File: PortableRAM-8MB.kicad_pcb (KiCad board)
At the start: 4 copper layers, 123 x 81 mm, 34 parts, among them J1 RAM Connector, J2 JTAG_Header_2.54mm_1x06, U1 ATF1502ASL, U10 AMS1117-3.3, U11 74HC245, U12 74HC245, U2 IS61WV5128BLL-10TLI, U3 IS61WV5128BLL-10TLI, U4 IS61WV5128BLL-10TLI, U5 IS61WV5128BLL-10TLI, U6 IS61WV5128BLL-10TLI, U7 IS61WV5128BLL-10TLI, U8 IS61WV5128BLL-10TLI, U9 IS61WV5128BLL-10TLI

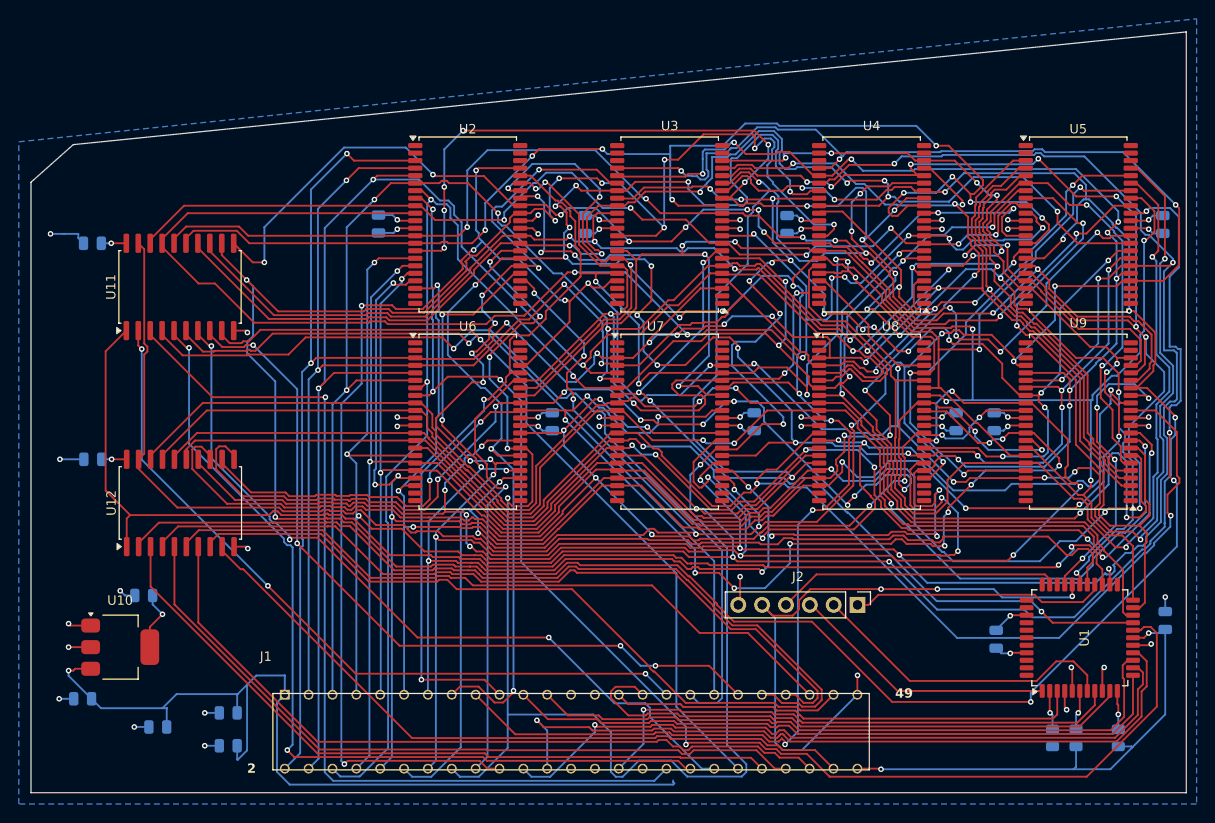
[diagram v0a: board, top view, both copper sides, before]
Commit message: PCB: strip all routing for fresh v2 layout, fix planes for all-5V
Clean canvas: all tracks and vias deleted; B.Cu +5V pour removed
(bottom layer freed for routing); In2 plane retargeted +3.3V -> +5V.
Preserved: proven board outline + angled corner, J1 position, the
edge-connector keepout, In1 GND plane, and all footprint placements
as a starting point. Next: Update PCB from Schematic, re-place as
needed, edge keepout, route.

Co-Authored-By: Claude Fable 5 <noreply@anthropic.com>
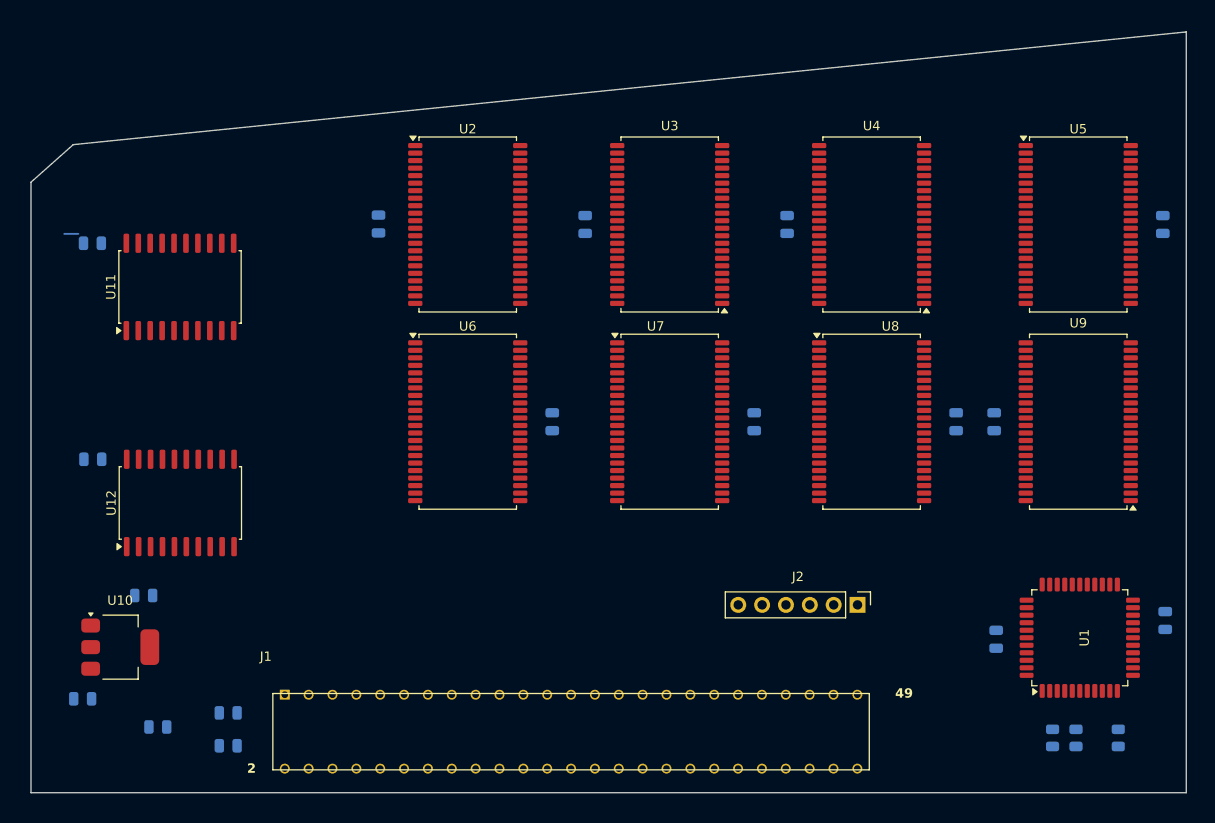
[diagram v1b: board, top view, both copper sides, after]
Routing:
- net /A13: track 316.4 -> 0.00 mm, vias 19 -> 0
- net /SD6: track 290.5 -> 0.00 mm, vias 13 -> 0
- net /A15: track 289.0 -> 0.00 mm, vias 23 -> 0
- net /A6: track 287.1 -> 0.00 mm, vias 12 -> 0
- net /A11: track 280.2 -> 0.00 mm, vias 16 -> 0
- net /A19: track 272.7 -> 0.00 mm, vias 14 -> 0
- net /A12: track 256.4 -> 0.00 mm, vias 19 -> 0
- net /A8: track 254.4 -> 0.00 mm, vias 12 -> 0
- net /A5: track 243.4 -> 0.00 mm, vias 10 -> 0
- net /A7: track 243.3 -> 0.00 mm, vias 9 -> 0
- net /A16: track 241.7 -> 0.00 mm, vias 12 -> 0
- net /A17: track 240.5 -> 0.00 mm, vias 9 -> 0
- net /A14: track 233.9 -> 0.00 mm, vias 19 -> 0
- net /A3: track 232.0 -> 0.00 mm, vias 6 -> 0
- net +5V: track 229.1 -> 0.00 mm, vias 12 -> 0
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- added copper zone on In2.Cu, net +5V
- removed copper zone on In2.Cu, net +3.3V
- removed copper zone on B.Cu, net +5V

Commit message: PCB: remove orphaned U10 (AMS1117) footprint
The LDO left the schematic in the all-5V conversion; the In2 plane
carries +5V directly, so v2 needs neither the part nor the v0.2
bridge trick. Footprint deleted from the board.

Co-Authored-By: Claude Fable 5 <noreply@anthropic.com>
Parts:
- removed U10: AMS1117-3.3, Package_TO_SOT_SMD:SOT-223-3_TabPin2

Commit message: PCB: uniform SRAM orientation + silkscreen population guide
- U3, U4, U9 rotated from 180 to 0: all eight SRAMs now face the same
  way (assembly-error prevention; free to do on the unrouted board)
- Silkscreen: '4+8MB' under U2/U3/U6/U7, '8MB only' under U4/U5/U8/U9,
  plus a two-line legend tying population to the JP1 jumper setting

Co-Authored-By: Claude Fable 5 <noreply@anthropic.com>
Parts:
- turned U3 to 0 degrees
- turned U4 to 0 degrees
- turned U9 to 0 degrees
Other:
- board text added: "4+8MB"
- board text added: "8MB only"
- board text added: "RAM SIZE — ALL 8 CHIPS = 8MB (JP1 OPEN)"
- board text added: "U2,U3,U6,U7 ONLY = 4MB (JP1 CLOSED)"

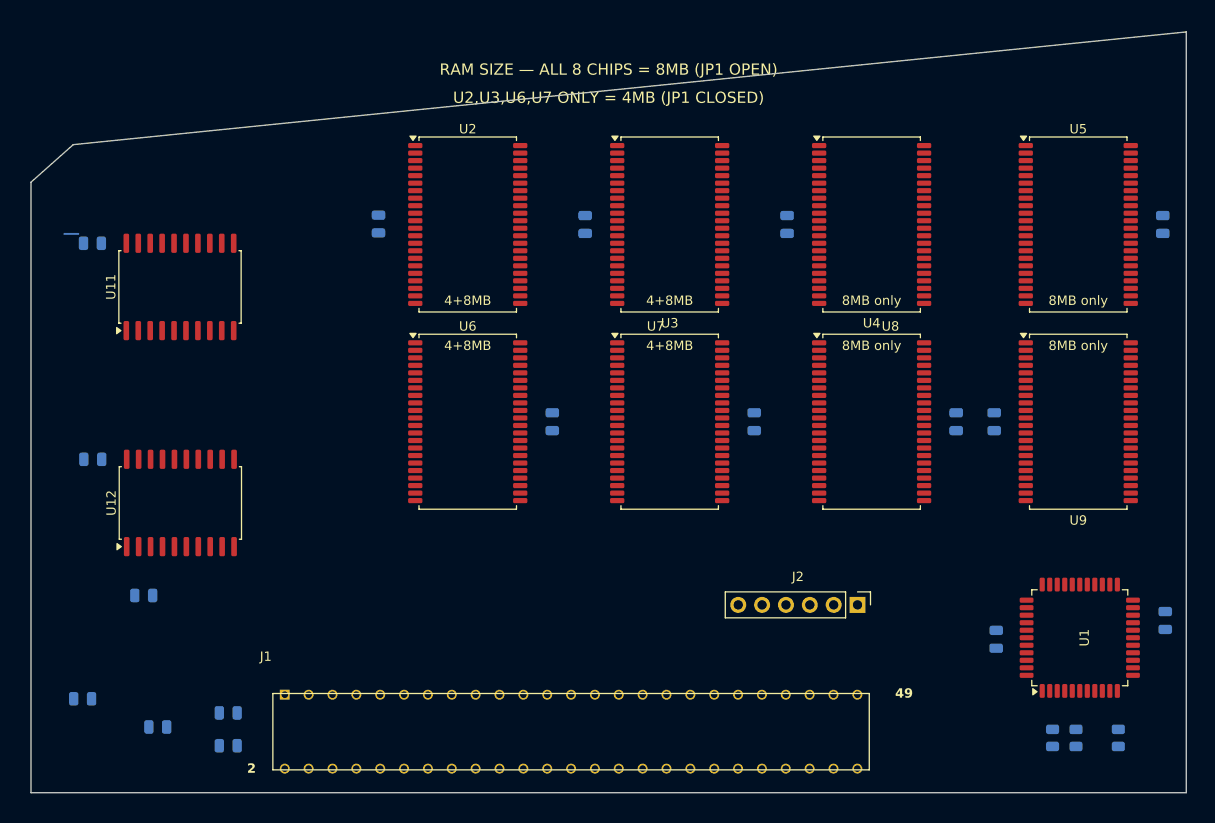
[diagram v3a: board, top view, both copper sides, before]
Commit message: PCB placement complete; WE net renamed WEL to match firmware
- Update PCB from Schematic applied: full v2 netlist on pads
  (WEL/WEH/BANKSEL/SIZE8), JP1/R5/C18/C19 placed
- All 100nF decouplers within 2.2-4.0mm of their power pins; all four
  CPLD VCC pins individually decoupled
- Bulk caps cover both J1 VCC pin clusters plus two points inside the
  memory array
- JP1+R5 config cluster at the accessible left edge
- DRC: no courtyard/placement conflicts

Co-Authored-By: Claude Fable 5 <noreply@anthropic.com>
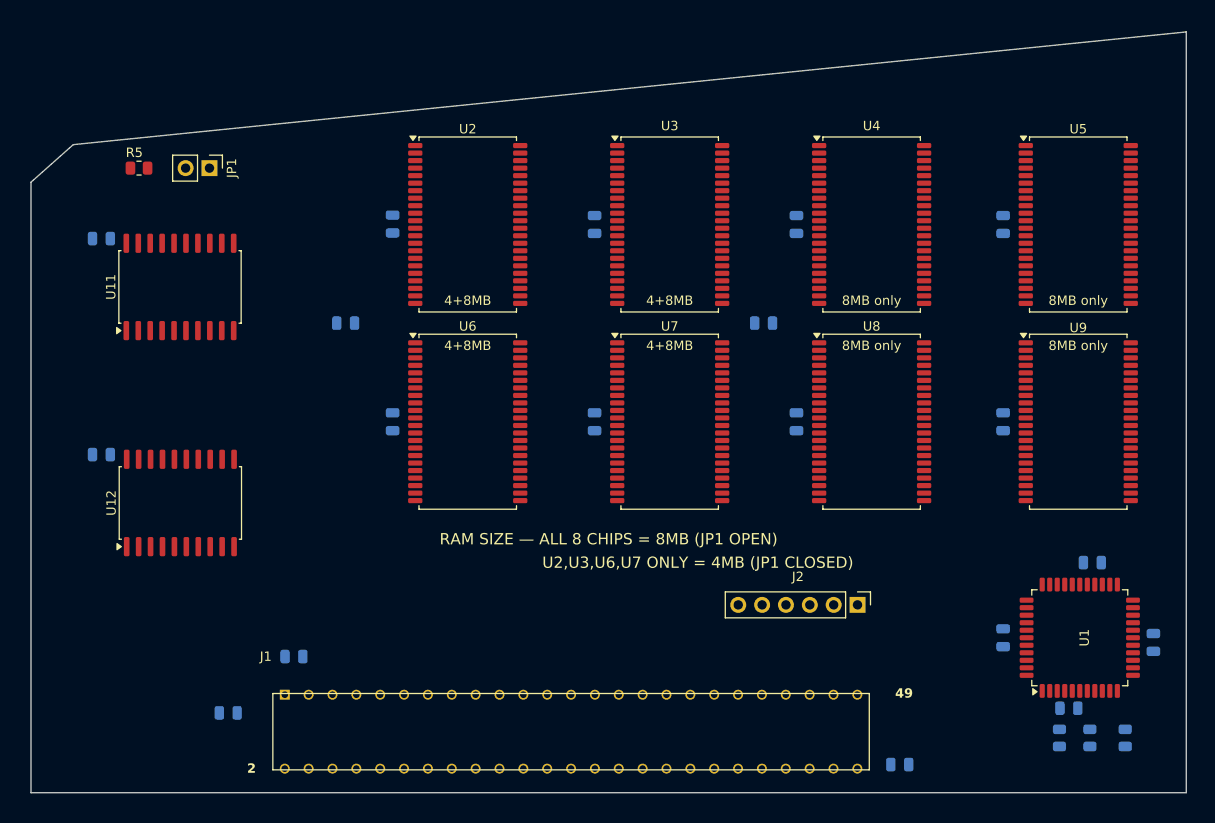
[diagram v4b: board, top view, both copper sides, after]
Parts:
- added C18: 100nF, Capacitor_SMD:C_0805_2012Metric, B.Cu at (188.0, 134.0)
- added C19: 10µF, Capacitor_SMD:C_0805_2012Metric, B.Cu at (96.5, 135.5)
- added JP1: SIZE: open=8MB closed=4MB, Connector_PinHeader_2.54mm:PinHeader_1x02_P2.54mm_Vertical, F.Cu at (87.5, 83.5)
- added R5: 10K, Resistor_SMD:R_0805_2012Metric, F.Cu at (80.0, 83.5)
- U2, U3, U4, U5, U6, U7, U8, U9: value IS61WV5128BLL-10TLI -> AS6C8008-55TIN
- moved C17 97.0 mm to (179.0, 141.0)
- moved C15 82.8 mm to (146.5, 100.0)
- moved C14 71.5 mm to (161.0, 147.0), turned to 0 degrees
- moved C16 36.1 mm to (102.0, 100.0)
- moved C1 17.0 mm to (172.0, 89.5), turned to -90 degrees
- moved C6 17.0 mm to (150.0, 110.5), turned to -90 degrees
- moved C7 17.0 mm to (128.5, 110.5), turned to -90 degrees
- moved C8 17.0 mm to (107.0, 110.5), turned to -90 degrees
- moved C9 9.91 mm to (181.5, 125.5), turned to 0 degrees
- moved C4 1.50 mm to (107.0, 89.5)
- moved R2 1.48 mm to (181.2, 144.2)
- moved C11 1.08 mm to (76.0, 91.0)
- moved C12 1.05 mm to (76.0, 114.0)
- moved C2 1.00 mm to (150.0, 89.5)
- moved C3 1.00 mm to (128.5, 89.5)
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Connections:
- C1 pad 1: +3.3V -> +5V
- C16 pad 1: +3.3V -> +5V
- C2 pad 1: +3.3V -> +5V
- C3 pad 1: +3.3V -> +5V
- C4 pad 1: +3.3V -> +5V
- C5 pad 1: +3.3V -> +5V
- C6 pad 1: +3.3V -> +5V
- C7 pad 1: +3.3V -> +5V
- C8 pad 1: +3.3V -> +5V
- U1 pad 28: /WE -> /WEL
- U1 pad 33: unconnected-(U1-I/O-Pad33) -> /BANKSEL
- U1 pad 34: unconnected-(U1-I/O-Pad34) -> /SIZE8
- U2 pad 1: unconnected-(U2-NC-Pad1) -> /A5
- U2 pad 11: +3.3V -> +5V
- U2 pad 15: /WE -> unconnected-(U2-NC-Pad15)
- U2 pad 16: /A6 -> unconnected-(U2-NC-Pad16)
- U2 pad 17: /A7 -> /WEL
- U2 pad 18: /A8 -> /BANKSEL
- U2 pad 19: /A9 -> /A19
- U2 pad 2: unconnected-(U2-NC-Pad2) -> /A4
- U2 pad 20: /A10 -> /A18
- U2 pad 21: unconnected-(U2-NC-Pad21) -> /A17
- U2 pad 22: unconnected-(U2-NC-Pad22) -> /A16
- U2 pad 23: unconnected-(U2-NC-Pad23) -> /A15
- U2 pad 24: unconnected-(U2-NC-Pad24) -> /A14
- U2 pad 25: unconnected-(U2-NC-Pad25) -> /A13
- U2 pad 26: /A11 -> /A12
- U2 pad 27: /A12 -> /A11
- U2 pad 28: /A13 -> /A10
- U2 pad 29: /A14 -> unconnected-(U2-NC-Pad29)
- U2 pad 3: /A1 -> /A3
- U2 pad 30: /A15 -> unconnected-(U2-NC-Pad30)
- U2 pad 33: +3.3V -> +5V
- U2 pad 37: /OE -> unconnected-(U2-NC-Pad37)
- U2 pad 38: /A16 -> unconnected-(U2-NC-Pad38)
- U2 pad 39: /A17 -> /A9
- U2 pad 40: /A18 -> +5V
- U2 pad 41: /A19 -> /OE
- U2 pad 42: unconnected-(U2-NC-Pad42) -> /A8
- U2 pad 43: unconnected-(U2-NC-Pad43) -> /A7
- U2 pad 44: unconnected-(U2-NC-Pad44) -> /A6
- U2 pad 5: /A3 -> /A1
- U2 pad 6: /A4 -> /CE0
- U2 pad 7: /A5 -> unconnected-(U2-NC-Pad7)
- U2 pad 8: /CE0 -> unconnected-(U2-NC-Pad8)
- U3 pad 1: unconnected-(U3-NC-Pad1) -> /A5
- U3 pad 11: +3.3V -> +5V
- U3 pad 15: /WE -> unconnected-(U3-NC-Pad15)
- U3 pad 16: /A6 -> unconnected-(U3-NC-Pad16)
- U3 pad 17: /A7 -> /WEL
- U3 pad 18: /A8 -> /BANKSEL
- U3 pad 19: /A9 -> /A19
- U3 pad 2: unconnected-(U3-NC-Pad2) -> /A4
- U3 pad 20: /A10 -> /A18
- U3 pad 21: unconnected-(U3-NC-Pad21) -> /A17
- U3 pad 22: unconnected-(U3-NC-Pad22) -> /A16
- U3 pad 23: unconnected-(U3-NC-Pad23) -> /A15
- U3 pad 24: unconnected-(U3-NC-Pad24) -> /A14
- U3 pad 25: unconnected-(U3-NC-Pad25) -> /A13
- U3 pad 26: /A11 -> /A12
- U3 pad 27: /A12 -> /A11
- U3 pad 28: /A13 -> /A10
- U3 pad 29: /A14 -> unconnected-(U3-NC-Pad29)
- U3 pad 3: /A1 -> /A3
- U3 pad 30: /A15 -> unconnected-(U3-NC-Pad30)
- U3 pad 33: +3.3V -> +5V
- U3 pad 37: /OE -> unconnected-(U3-NC-Pad37)
- U3 pad 38: /A16 -> unconnected-(U3-NC-Pad38)
- U3 pad 39: /A17 -> /A9
- U3 pad 40: /A18 -> +5V
- U3 pad 41: /A19 -> /OE
- U3 pad 42: unconnected-(U3-NC-Pad42) -> /A8
- U3 pad 43: unconnected-(U3-NC-Pad43) -> /A7
- U3 pad 44: unconnected-(U3-NC-Pad44) -> /A6
- U3 pad 5: /A3 -> /A1
- U3 pad 6: /A4 -> /CE1
- U3 pad 7: /A5 -> unconnected-(U3-NC-Pad7)
- U3 pad 8: /CE1 -> unconnected-(U3-NC-Pad8)
- U4 pad 1: unconnected-(U4-NC-Pad1) -> /A5
- U4 pad 11: +3.3V -> +5V
- U4 pad 15: /WE -> unconnected-(U4-NC-Pad15)
- U4 pad 16: /A6 -> unconnected-(U4-NC-Pad16)
- U4 pad 17: /A7 -> /WEL
- U4 pad 18: /A8 -> /BANKSEL
- U4 pad 19: /A9 -> /A19
- U4 pad 2: unconnected-(U4-NC-Pad2) -> /A4
- U4 pad 20: /A10 -> /A18
- U4 pad 21: unconnected-(U4-NC-Pad21) -> /A17
- U4 pad 22: unconnected-(U4-NC-Pad22) -> /A16
- U4 pad 23: unconnected-(U4-NC-Pad23) -> /A15
- U4 pad 24: unconnected-(U4-NC-Pad24) -> /A14
- U4 pad 25: unconnected-(U4-NC-Pad25) -> /A13
- U4 pad 26: /A11 -> /A12
- U4 pad 27: /A12 -> /A11
- U4 pad 28: /A13 -> /A10
- U4 pad 29: /A14 -> unconnected-(U4-NC-Pad29)
- U4 pad 3: /A1 -> /A3
- U4 pad 30: /A15 -> unconnected-(U4-NC-Pad30)
- U4 pad 33: +3.3V -> +5V
- U4 pad 37: /OE -> unconnected-(U4-NC-Pad37)
- U4 pad 38: /A16 -> unconnected-(U4-NC-Pad38)
- U4 pad 39: /A17 -> /A9
- U4 pad 40: /A18 -> +5V
- U4 pad 41: /A19 -> /OE
- U4 pad 42: unconnected-(U4-NC-Pad42) -> /A8
- U4 pad 43: unconnected-(U4-NC-Pad43) -> /A7
- U4 pad 44: unconnected-(U4-NC-Pad44) -> /A6
- U4 pad 5: /A3 -> /A1
- U4 pad 6: /A4 -> /CE2
- U4 pad 7: /A5 -> unconnected-(U4-NC-Pad7)
- U4 pad 8: /CE2 -> unconnected-(U4-NC-Pad8)
- U5 pad 1: unconnected-(U5-NC-Pad1) -> /A5
- U5 pad 11: +3.3V -> +5V
- U5 pad 15: /WE -> unconnected-(U5-NC-Pad15)
- U5 pad 16: /A6 -> unconnected-(U5-NC-Pad16)
- U5 pad 17: /A7 -> /WEL
- U5 pad 18: /A8 -> /BANKSEL
- U5 pad 19: /A9 -> /A19
- U5 pad 2: unconnected-(U5-NC-Pad2) -> /A4
- U5 pad 20: /A10 -> /A18
- U5 pad 21: unconnected-(U5-NC-Pad21) -> /A17
- U5 pad 22: unconnected-(U5-NC-Pad22) -> /A16
- U5 pad 23: unconnected-(U5-NC-Pad23) -> /A15
- U5 pad 24: unconnected-(U5-NC-Pad24) -> /A14
- U5 pad 25: unconnected-(U5-NC-Pad25) -> /A13
- U5 pad 26: /A11 -> /A12
- U5 pad 27: /A12 -> /A11
- U5 pad 28: /A13 -> /A10
- U5 pad 29: /A14 -> unconnected-(U5-NC-Pad29)
- U5 pad 3: /A1 -> /A3
- U5 pad 30: /A15 -> unconnected-(U5-NC-Pad30)
- U5 pad 33: +3.3V -> +5V
- U5 pad 37: /OE -> unconnected-(U5-NC-Pad37)
- U5 pad 38: /A16 -> unconnected-(U5-NC-Pad38)
- U5 pad 39: /A17 -> /A9
- U5 pad 40: /A18 -> +5V
- U5 pad 41: /A19 -> /OE
- U5 pad 42: unconnected-(U5-NC-Pad42) -> /A8
- U5 pad 43: unconnected-(U5-NC-Pad43) -> /A7
- U5 pad 44: unconnected-(U5-NC-Pad44) -> /A6
- U5 pad 5: /A3 -> /A1
- U5 pad 6: /A4 -> /CE3
- U5 pad 7: /A5 -> unconnected-(U5-NC-Pad7)
- U5 pad 8: /CE3 -> unconnected-(U5-NC-Pad8)
- U6 pad 1: unconnected-(U6-NC-Pad1) -> /A5
- U6 pad 11: +3.3V -> +5V
- U6 pad 15: /WEH -> unconnected-(U6-NC-Pad15)
- U6 pad 16: /A6 -> unconnected-(U6-NC-Pad16)
- U6 pad 17: /A7 -> /WEH
- U6 pad 18: /A8 -> /BANKSEL
- U6 pad 19: /A9 -> /A19
- U6 pad 2: unconnected-(U6-NC-Pad2) -> /A4
- U6 pad 20: /A10 -> /A18
- U6 pad 21: unconnected-(U6-NC-Pad21) -> /A17
- U6 pad 22: unconnected-(U6-NC-Pad22) -> /A16
- U6 pad 23: unconnected-(U6-NC-Pad23) -> /A15
- U6 pad 24: unconnected-(U6-NC-Pad24) -> /A14
- U6 pad 25: unconnected-(U6-NC-Pad25) -> /A13
- U6 pad 26: /A11 -> /A12
- U6 pad 27: /A12 -> /A11
- U6 pad 28: /A13 -> /A10
- U6 pad 29: /A14 -> unconnected-(U6-NC-Pad29)
- U6 pad 3: /A1 -> /A3
- U6 pad 30: /A15 -> unconnected-(U6-NC-Pad30)
- U6 pad 33: +3.3V -> +5V
- U6 pad 37: /OE -> unconnected-(U6-NC-Pad37)
- U6 pad 38: /A16 -> unconnected-(U6-NC-Pad38)
- U6 pad 39: /A17 -> /A9
- U6 pad 40: /A18 -> +5V
- U6 pad 41: /A19 -> /OE
- U6 pad 42: unconnected-(U6-NC-Pad42) -> /A8
- U6 pad 43: unconnected-(U6-NC-Pad43) -> /A7
- U6 pad 44: unconnected-(U6-NC-Pad44) -> /A6
- U6 pad 5: /A3 -> /A1
- U6 pad 6: /A4 -> /CE0
- U6 pad 7: /A5 -> unconnected-(U6-NC-Pad7)
- U6 pad 8: /CE0 -> unconnected-(U6-NC-Pad8)
- U7 pad 1: unconnected-(U7-NC-Pad1) -> /A5
- U7 pad 11: +3.3V -> +5V
- U7 pad 15: /WEH -> unconnected-(U7-NC-Pad15)
- U7 pad 16: /A6 -> unconnected-(U7-NC-Pad16)
- U7 pad 17: /A7 -> /WEH
- U7 pad 18: /A8 -> /BANKSEL
- U7 pad 19: /A9 -> /A19
- U7 pad 2: unconnected-(U7-NC-Pad2) -> /A4
- U7 pad 20: /A10 -> /A18
- U7 pad 21: unconnected-(U7-NC-Pad21) -> /A17
- U7 pad 22: unconnected-(U7-NC-Pad22) -> /A16
- U7 pad 23: unconnected-(U7-NC-Pad23) -> /A15
- U7 pad 24: unconnected-(U7-NC-Pad24) -> /A14
- U7 pad 25: unconnected-(U7-NC-Pad25) -> /A13
- U7 pad 26: /A11 -> /A12
- U7 pad 27: /A12 -> /A11
- U7 pad 28: /A13 -> /A10
- U7 pad 29: /A14 -> unconnected-(U7-NC-Pad29)
- U7 pad 3: /A1 -> /A3
- U7 pad 30: /A15 -> unconnected-(U7-NC-Pad30)
- U7 pad 33: +3.3V -> +5V
- U7 pad 37: /OE -> unconnected-(U7-NC-Pad37)
- U7 pad 38: /A16 -> unconnected-(U7-NC-Pad38)
- U7 pad 39: /A17 -> /A9
- U7 pad 40: /A18 -> +5V
- U7 pad 41: /A19 -> /OE
- U7 pad 42: unconnected-(U7-NC-Pad42) -> /A8
- U7 pad 43: unconnected-(U7-NC-Pad43) -> /A7
- U7 pad 44: unconnected-(U7-NC-Pad44) -> /A6
- U7 pad 5: /A3 -> /A1
- U7 pad 6: /A4 -> /CE1
- U7 pad 7: /A5 -> unconnected-(U7-NC-Pad7)
- U7 pad 8: /CE1 -> unconnected-(U7-NC-Pad8)
- U8 pad 1: unconnected-(U8-NC-Pad1) -> /A5
- U8 pad 11: +3.3V -> +5V
- U8 pad 15: /WEH -> unconnected-(U8-NC-Pad15)
- U8 pad 16: /A6 -> unconnected-(U8-NC-Pad16)
- U8 pad 17: /A7 -> /WEH
- U8 pad 18: /A8 -> /BANKSEL
- U8 pad 19: /A9 -> /A19
- U8 pad 2: unconnected-(U8-NC-Pad2) -> /A4
- U8 pad 20: /A10 -> /A18
- U8 pad 21: unconnected-(U8-NC-Pad21) -> /A17
- U8 pad 22: unconnected-(U8-NC-Pad22) -> /A16
- U8 pad 23: unconnected-(U8-NC-Pad23) -> /A15
- U8 pad 24: unconnected-(U8-NC-Pad24) -> /A14
- U8 pad 25: unconnected-(U8-NC-Pad25) -> /A13
- U8 pad 26: /A11 -> /A12
- U8 pad 27: /A12 -> /A11
- U8 pad 28: /A13 -> /A10
- U8 pad 29: /A14 -> unconnected-(U8-NC-Pad29)
- U8 pad 3: /A1 -> /A3
- U8 pad 30: /A15 -> unconnected-(U8-NC-Pad30)
- U8 pad 33: +3.3V -> +5V
- U8 pad 37: /OE -> unconnected-(U8-NC-Pad37)
- U8 pad 38: /A16 -> unconnected-(U8-NC-Pad38)
- U8 pad 39: /A17 -> /A9
- U8 pad 40: /A18 -> +5V
- U8 pad 41: /A19 -> /OE
- U8 pad 42: unconnected-(U8-NC-Pad42) -> /A8
- U8 pad 43: unconnected-(U8-NC-Pad43) -> /A7
- U8 pad 44: unconnected-(U8-NC-Pad44) -> /A6
- U8 pad 5: /A3 -> /A1
- U8 pad 6: /A4 -> /CE2
- U8 pad 7: /A5 -> unconnected-(U8-NC-Pad7)
- U8 pad 8: /CE2 -> unconnected-(U8-NC-Pad8)
- U9 pad 1: unconnected-(U9-NC-Pad1) -> /A5
- U9 pad 11: +3.3V -> +5V
- U9 pad 15: /WEH -> unconnected-(U9-NC-Pad15)
- U9 pad 16: /A6 -> unconnected-(U9-NC-Pad16)
- U9 pad 17: /A7 -> /WEH
- U9 pad 18: /A8 -> /BANKSEL
- U9 pad 19: /A9 -> /A19
- U9 pad 2: unconnected-(U9-NC-Pad2) -> /A4
- U9 pad 20: /A10 -> /A18
- U9 pad 21: unconnected-(U9-NC-Pad21) -> /A17
- U9 pad 22: unconnected-(U9-NC-Pad22) -> /A16
- U9 pad 23: unconnected-(U9-NC-Pad23) -> /A15
- U9 pad 24: unconnected-(U9-NC-Pad24) -> /A14
- U9 pad 25: unconnected-(U9-NC-Pad25) -> /A13
- U9 pad 26: /A11 -> /A12
- U9 pad 27: /A12 -> /A11
- U9 pad 28: /A13 -> /A10
- U9 pad 29: /A14 -> unconnected-(U9-NC-Pad29)
- U9 pad 3: /A1 -> /A3
- U9 pad 30: /A15 -> unconnected-(U9-NC-Pad30)
- U9 pad 33: +3.3V -> +5V
- U9 pad 37: /OE -> unconnected-(U9-NC-Pad37)
- U9 pad 38: /A16 -> unconnected-(U9-NC-Pad38)
- U9 pad 39: /A17 -> /A9
- U9 pad 40: /A18 -> +5V
- U9 pad 41: /A19 -> /OE
- U9 pad 42: unconnected-(U9-NC-Pad42) -> /A8
- U9 pad 43: unconnected-(U9-NC-Pad43) -> /A7
- U9 pad 44: unconnected-(U9-NC-Pad44) -> /A6
- U9 pad 5: /A3 -> /A1
- U9 pad 6: /A4 -> /CE3
- U9 pad 7: /A5 -> unconnected-(U9-NC-Pad7)
- U9 pad 8: /CE3 -> unconnected-(U9-NC-Pad8)

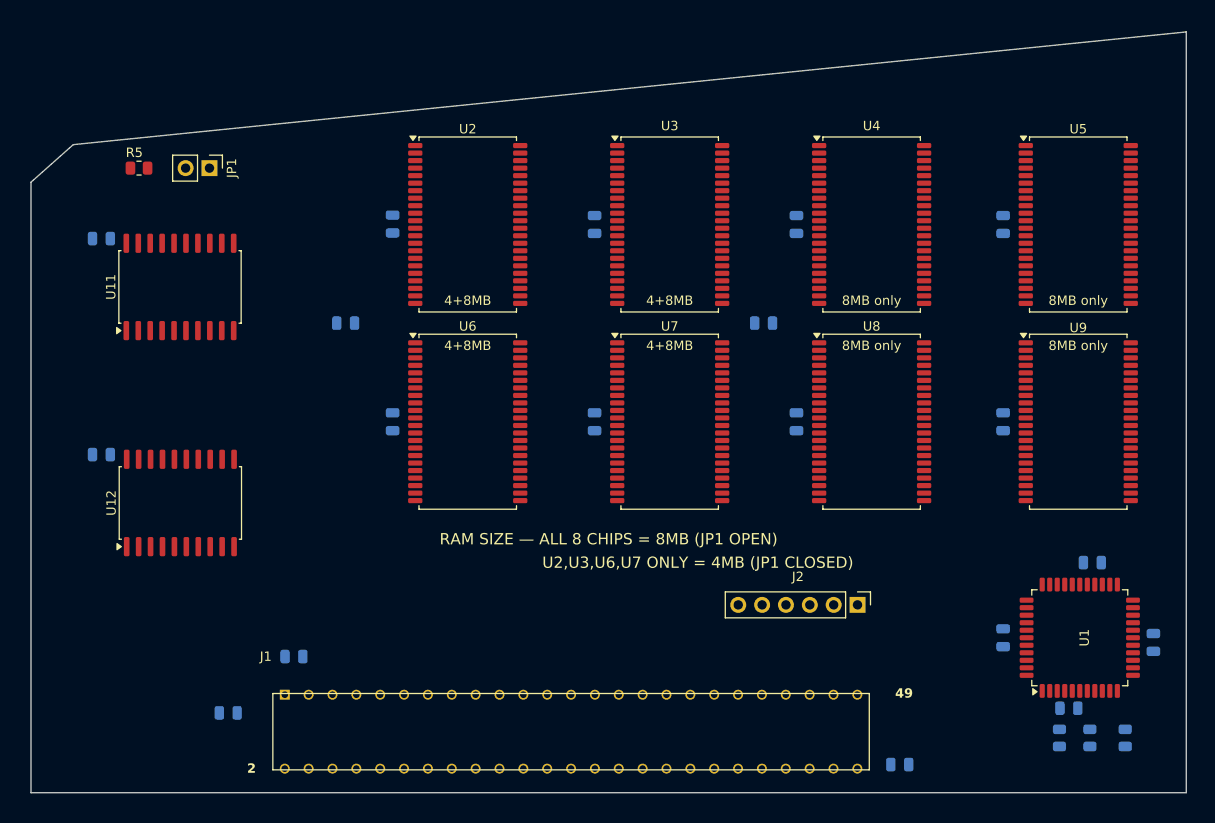
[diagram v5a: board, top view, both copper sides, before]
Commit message: PCB: power/ground stitching complete
Every SMD power and ground pad via'd to its plane (In2=+5V, In1=GND):
SRAM pins 11/12 plus the 33/34 anchor pads and the critical CS2 (pad
40) active-high enable on all 8 chips, CPLD's 4+4 power pins, both
'245s, and all 19 decoupling/bulk caps. DRC: 0 power/GND pads
floating; only the 283 signal-net ratsnest remains for routing.

Co-Authored-By: Claude Fable 5 <noreply@anthropic.com>
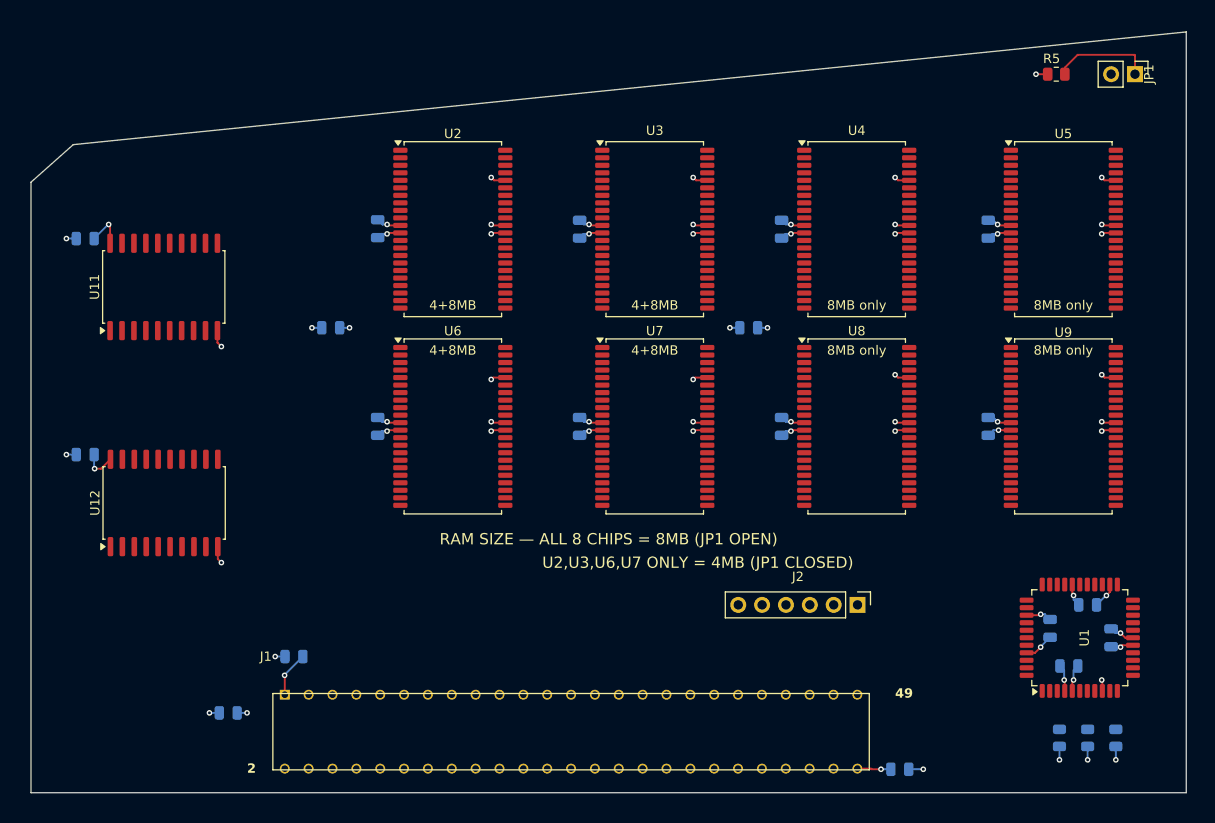
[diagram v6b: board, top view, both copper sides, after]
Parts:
- moved JP1 99.0 mm to (186.0, 73.5)
- moved R5 98.2 mm to (177.7, 73.5)
- moved C10 5.10 mm to (177.0, 132.5)
- moved C18 4.53 mm to (183.5, 133.5)
- moved C9 4.53 mm to (181.0, 130.0)
- moved C17 4.50 mm to (179.0, 136.5)
- moved C11 1.73 mm to (74.3, 91.0)
- moved C12 1.73 mm to (74.3, 114.0)
- moved U12 1.73 mm to (82.7, 119.2)
- moved U11 1.73 mm to (82.6, 96.2)
- moved C1 1.66 mm to (170.4, 90.0)
- moved C15 1.66 mm to (144.9, 100.5)
- moved C16 1.66 mm to (100.4, 100.5)
- moved C2 1.66 mm to (148.4, 90.0)
- moved C3 1.66 mm to (126.9, 90.0)
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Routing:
- net +5V: track 0.00 -> 84.0 mm, vias 0 -> 40
- net GND: track 0.00 -> 56.0 mm, vias 0 -> 29
- net /SIZE8: track 0.00 -> 10.8 mm
